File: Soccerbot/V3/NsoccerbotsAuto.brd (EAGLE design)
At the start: 149.8 x 101.3 mm, 69 parts, among them CN2 1X4-CLEANBIG, IC1 LM340S-05, IC2 TB6612FNG, IC4 TB6612FNG, J3 1X5, J4 1X5, Q1 AOD417, SW2 SPST_TACT-EVQQ2, U1 PCA9685, X1 NXT-SOCKET, X2 NXT-SOCKET, X3 NXT-SOCKET, X4 NXT-SOCKET

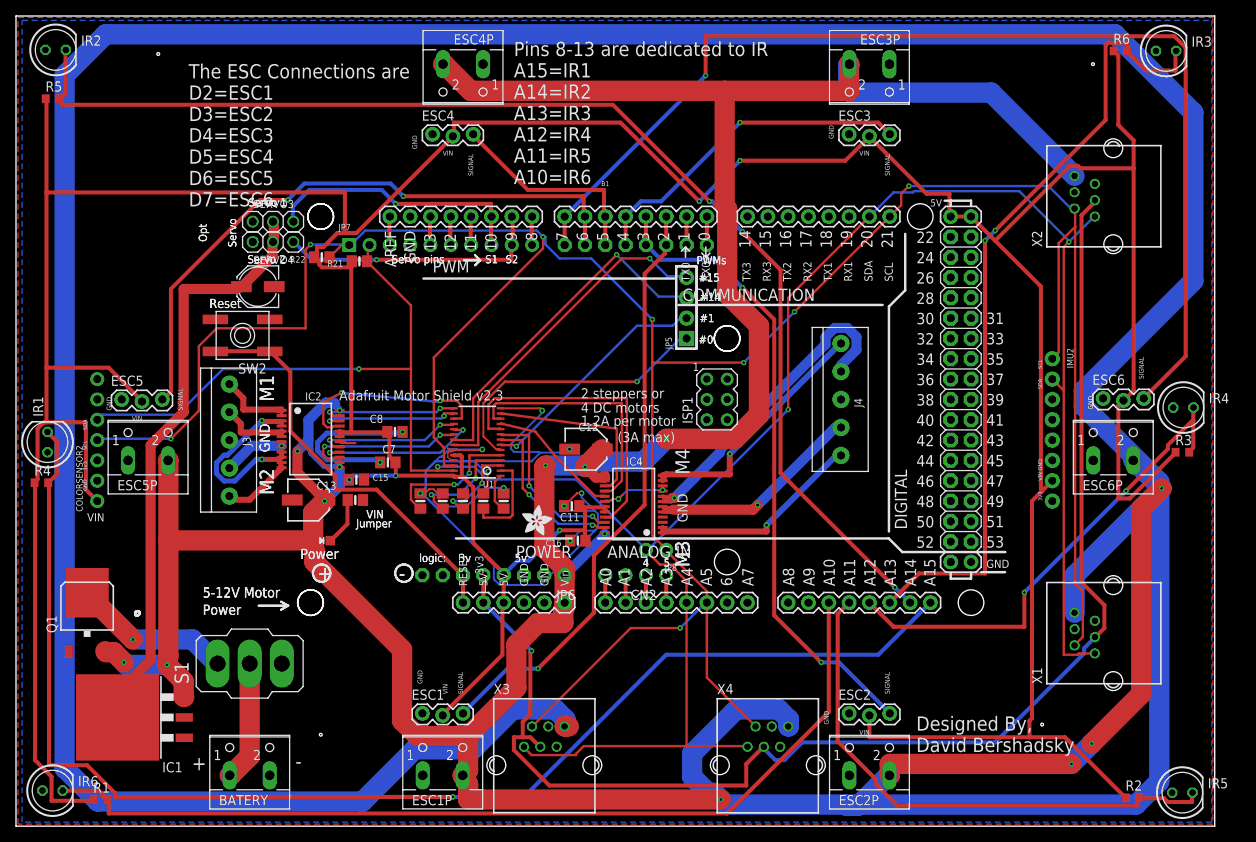
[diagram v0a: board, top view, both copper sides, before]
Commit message: Fully routed and all parts in
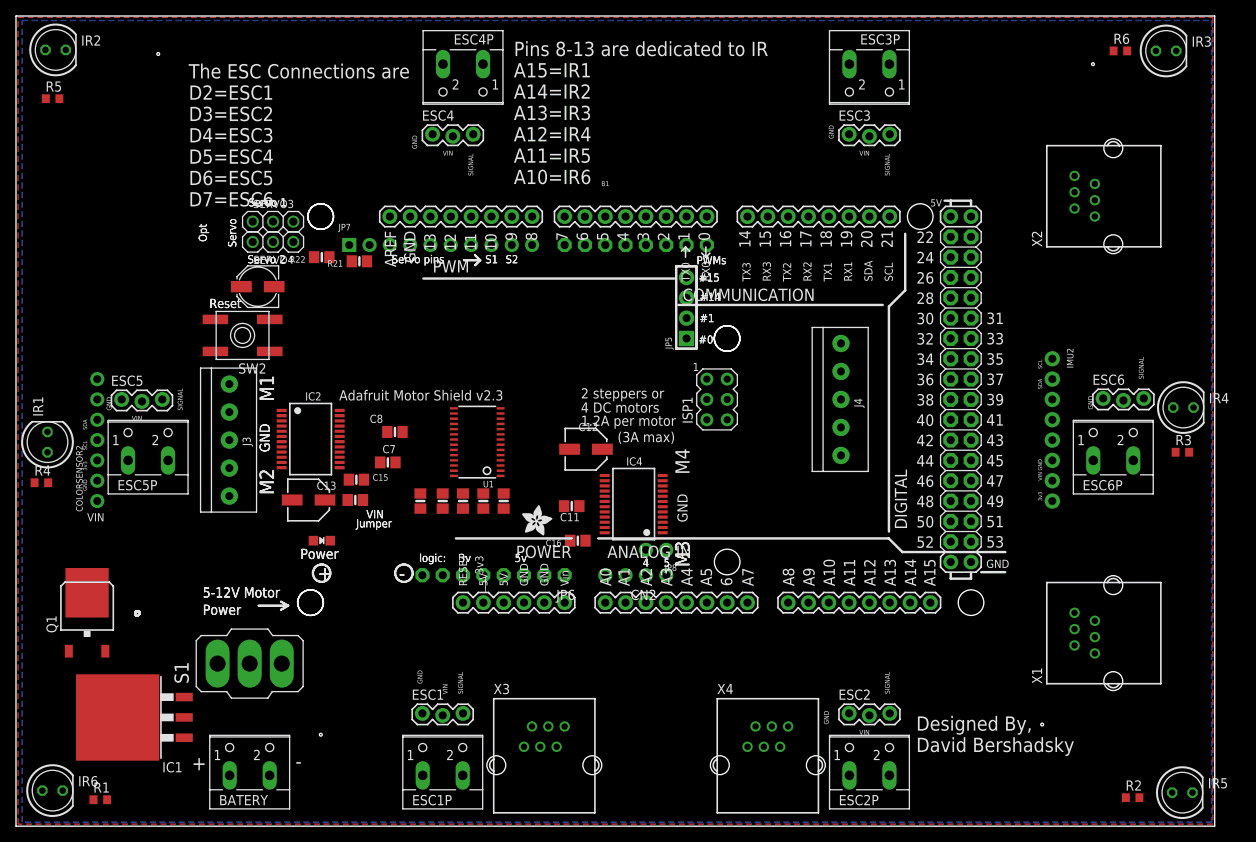
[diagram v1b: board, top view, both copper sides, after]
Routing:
- net BAT+: track 969.7 -> 0.00 mm, vias 14 -> 0
- net 5.5V: track 581.7 -> 0.00 mm, vias 5 -> 0
- net SCL: track 356.9 -> 0.00 mm, vias 8 -> 0
- net SDA: track 310.2 -> 0.00 mm, vias 4 -> 0
- net GND: track 185.0 -> 0.00 mm, vias 15 -> 0
- net 3.3V: track 171.3 -> 0.00 mm, vias 1 -> 0
- net A15: track 164.7 -> 0.00 mm, vias 1 -> 0
- net A14: track 154.1 -> 0.00 mm, vias 3 -> 0
- net D7: track 140.0 -> 0.00 mm, vias 1 -> 0
- net A10: track 116.9 -> 0.00 mm
- net A13: track 99.2 -> 0.00 mm, vias 2 -> 0
- net D3: track 80.0 -> 0.00 mm, vias 2 -> 0
- net D6: track 78.2 -> 0.00 mm, vias 2 -> 0
- net D2: track 74.9 -> 0.00 mm, vias 1 -> 0
- net SERVO5V: track 74.2 -> 0.00 mm
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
